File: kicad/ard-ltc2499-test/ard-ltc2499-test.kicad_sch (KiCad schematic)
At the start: 40 parts, among them P1 Power, P2 Analog, P3 Digital, P4 Digital, P5 CONN_01X01, P6 CONN_01X01, P7 CONN_01X01, P8 CONN_01X01, U1 LT6654xxS6-1.25, U2 LT6654xxS6-2.5

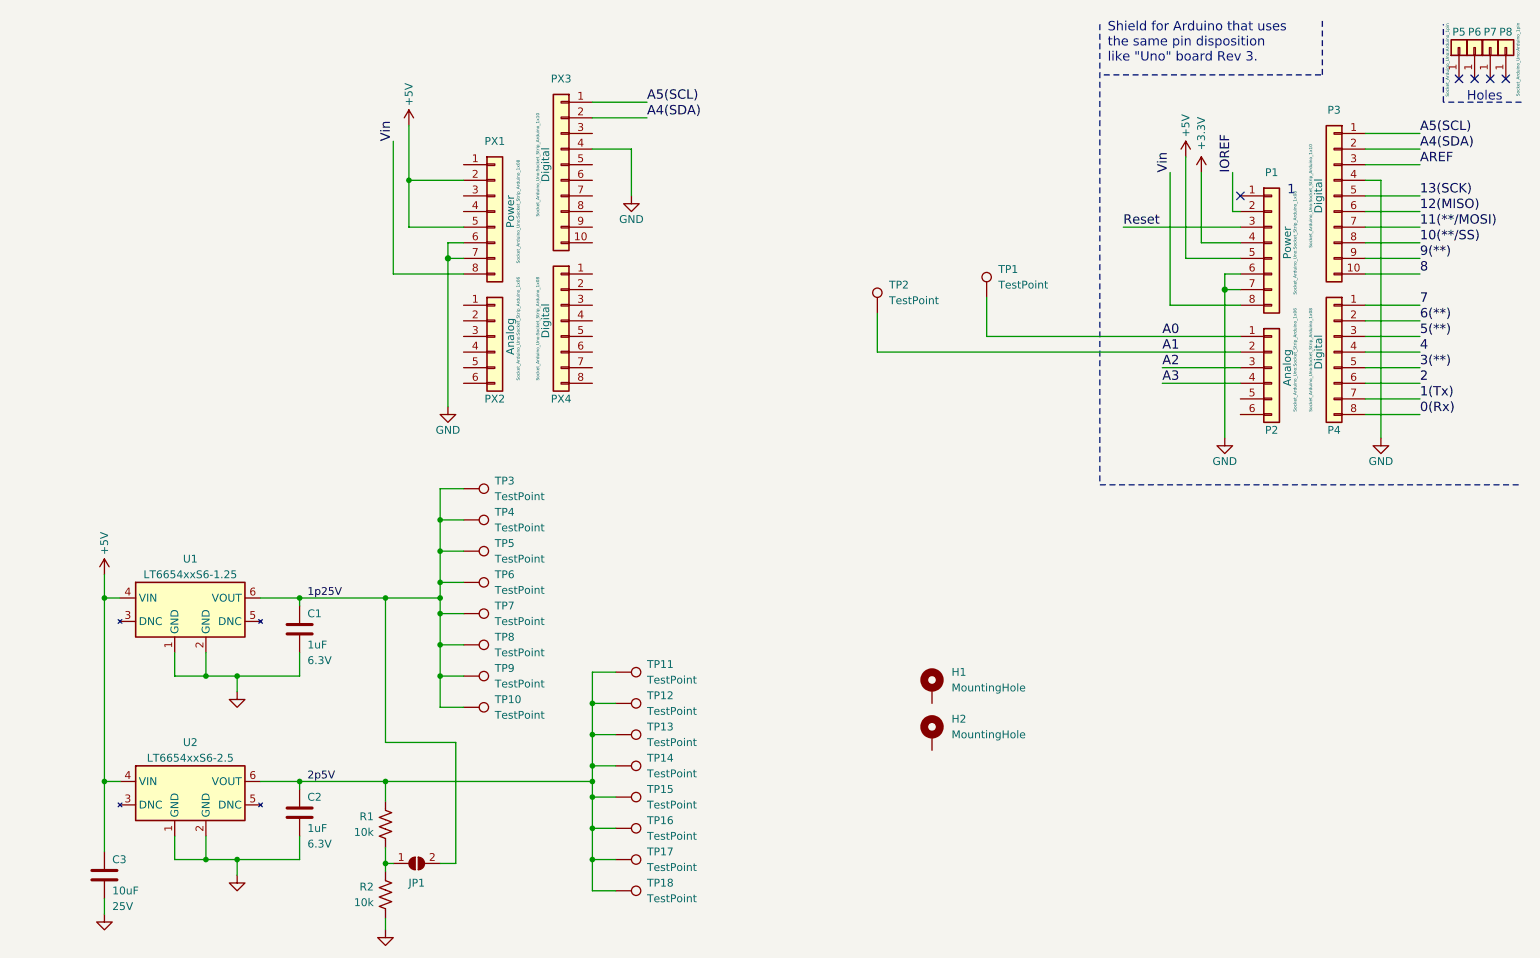
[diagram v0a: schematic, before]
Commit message: Added 5V divider and moved refernce divider to 1.25V
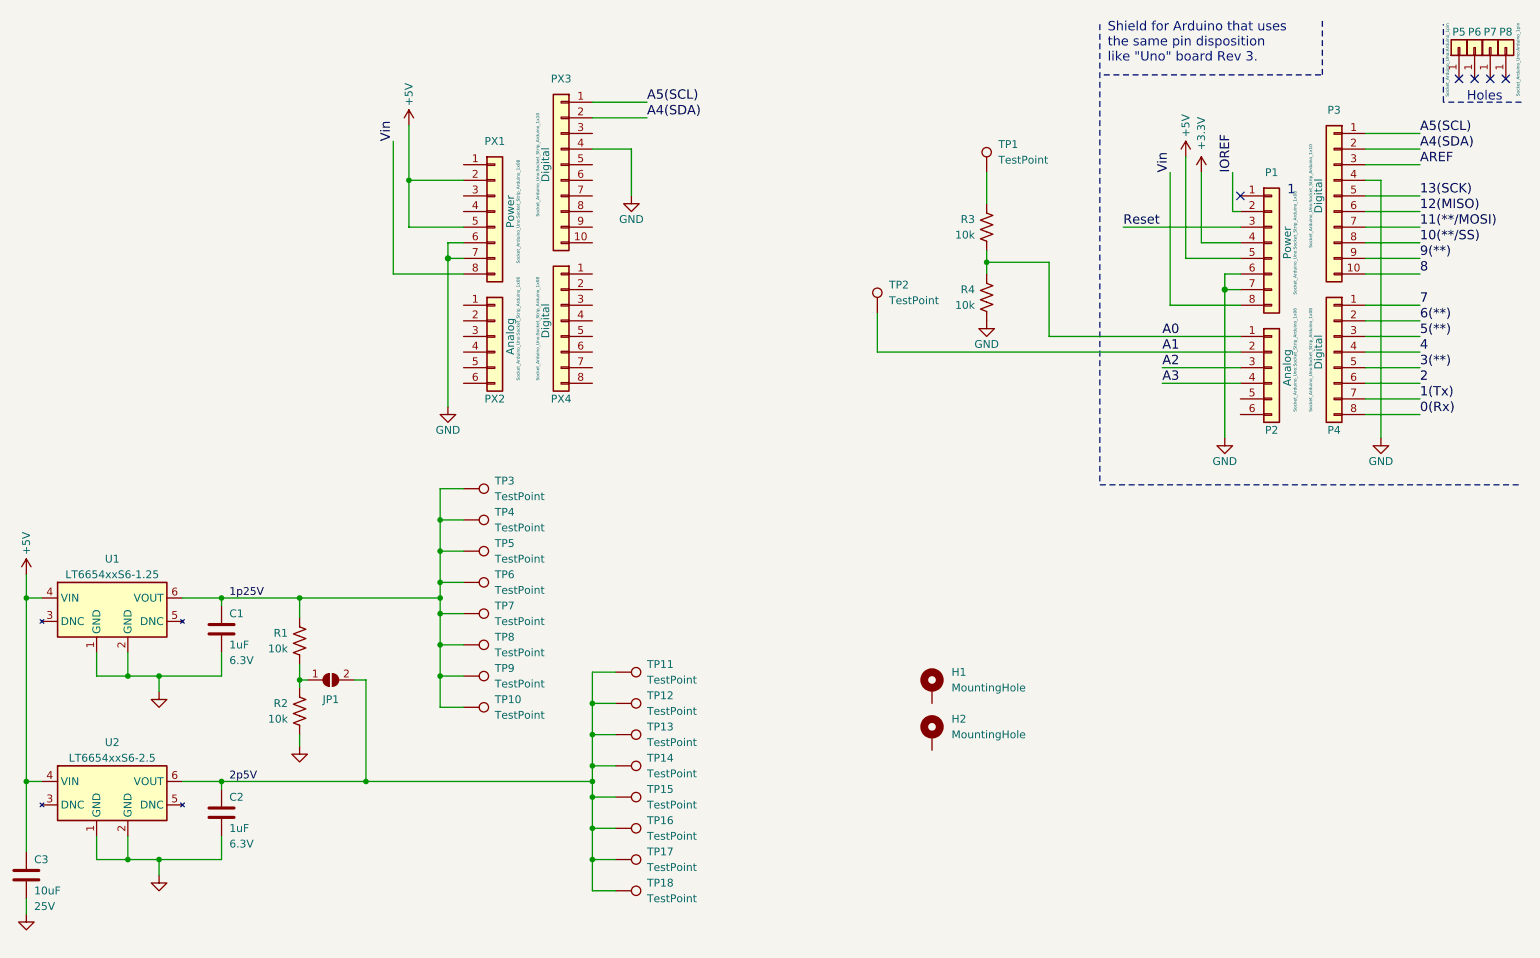
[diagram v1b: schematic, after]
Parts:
- added R3, R4: 10k, Resistor_SMD:R_0805_2012Metric, symbol Device:R_US
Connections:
- net 1p25V: now also R1.2; no longer JP1.2 (B)
- net 2p5V: now also JP1.2 (B); no longer R1.2
- net A0: now also R3.1, R4.2; no longer TP1.1
- net GND: now also R4.1
- new net: R3.2, TP1.1
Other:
- moved on the sheet: C1, C2, C3, JP1, R1, R2, TP1, U1, U2
